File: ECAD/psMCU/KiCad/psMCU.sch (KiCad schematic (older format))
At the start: 0 parts

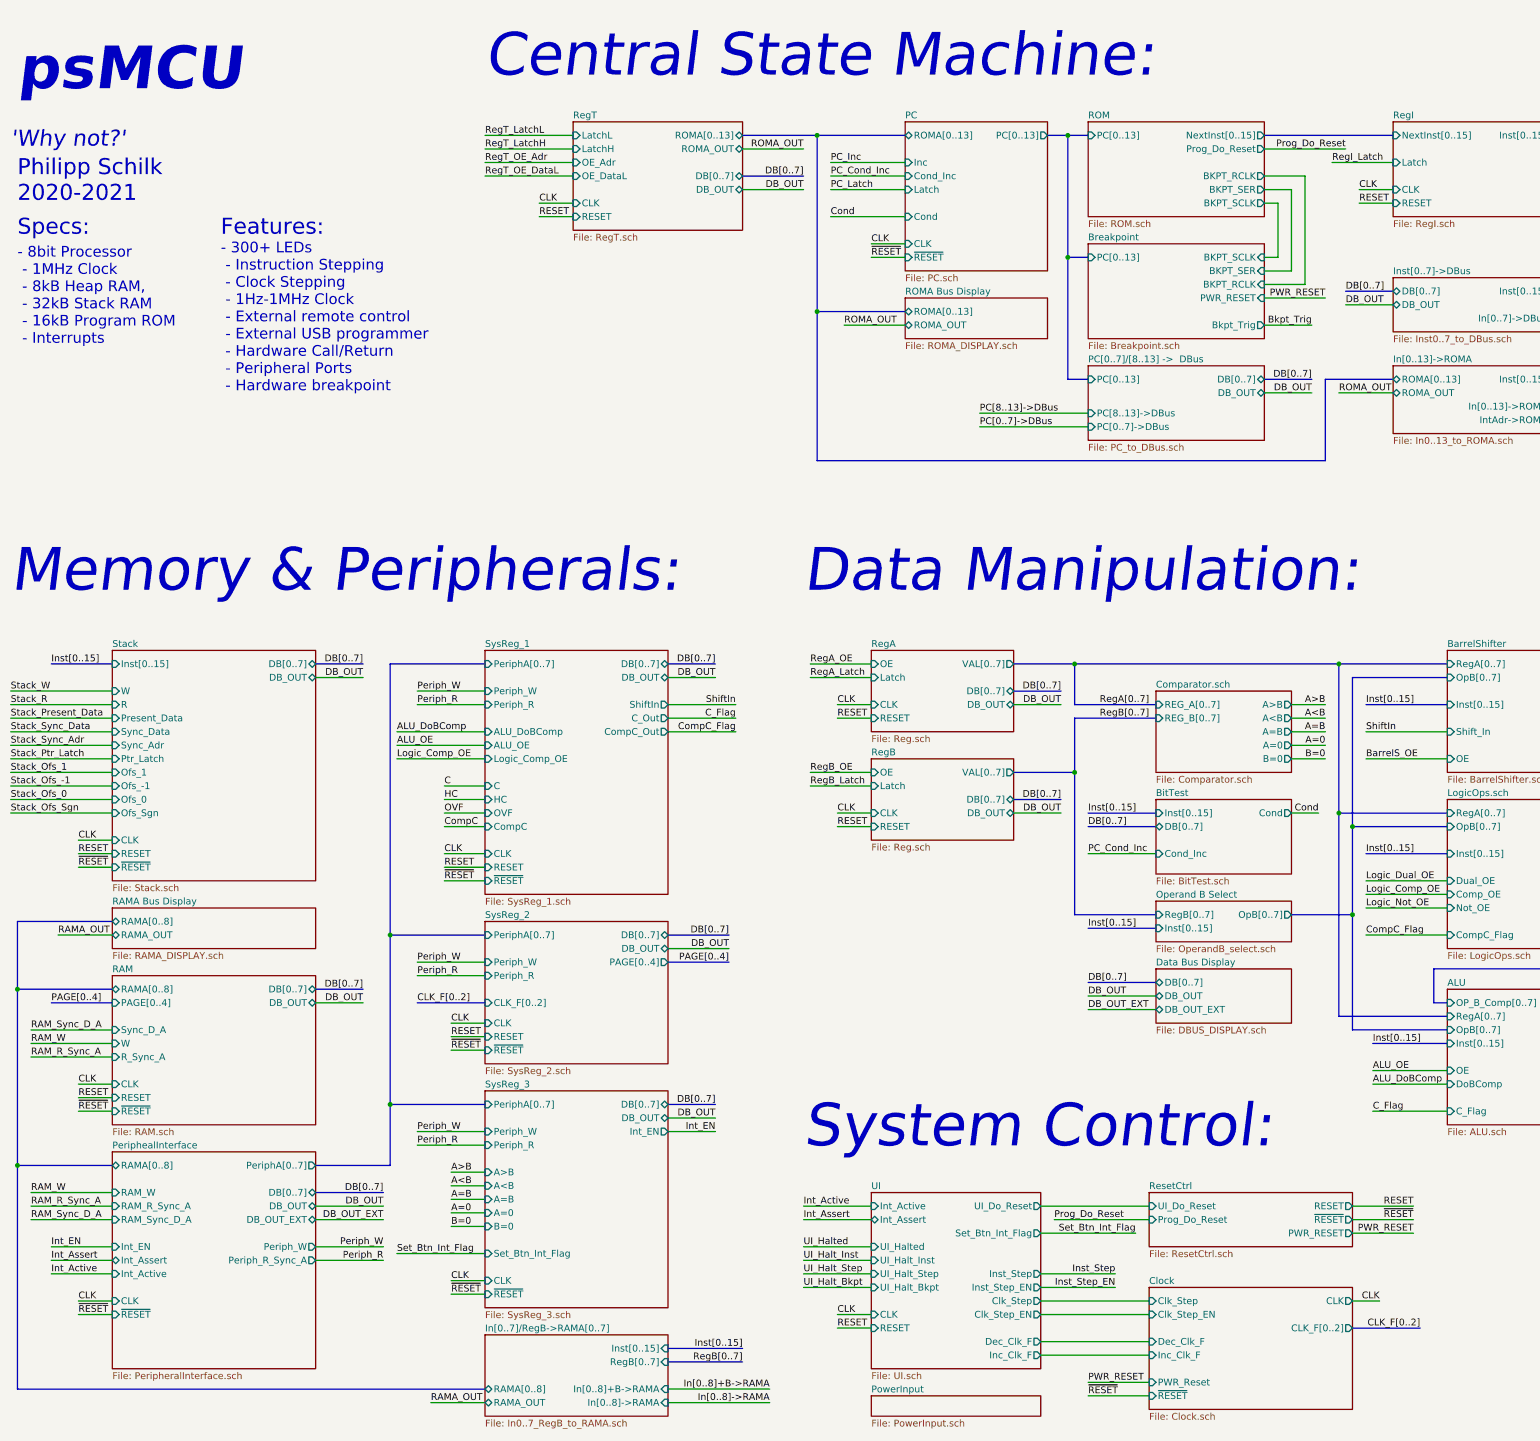
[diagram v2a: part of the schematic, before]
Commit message: Sch: Increased RAM page count, changed SYS registers
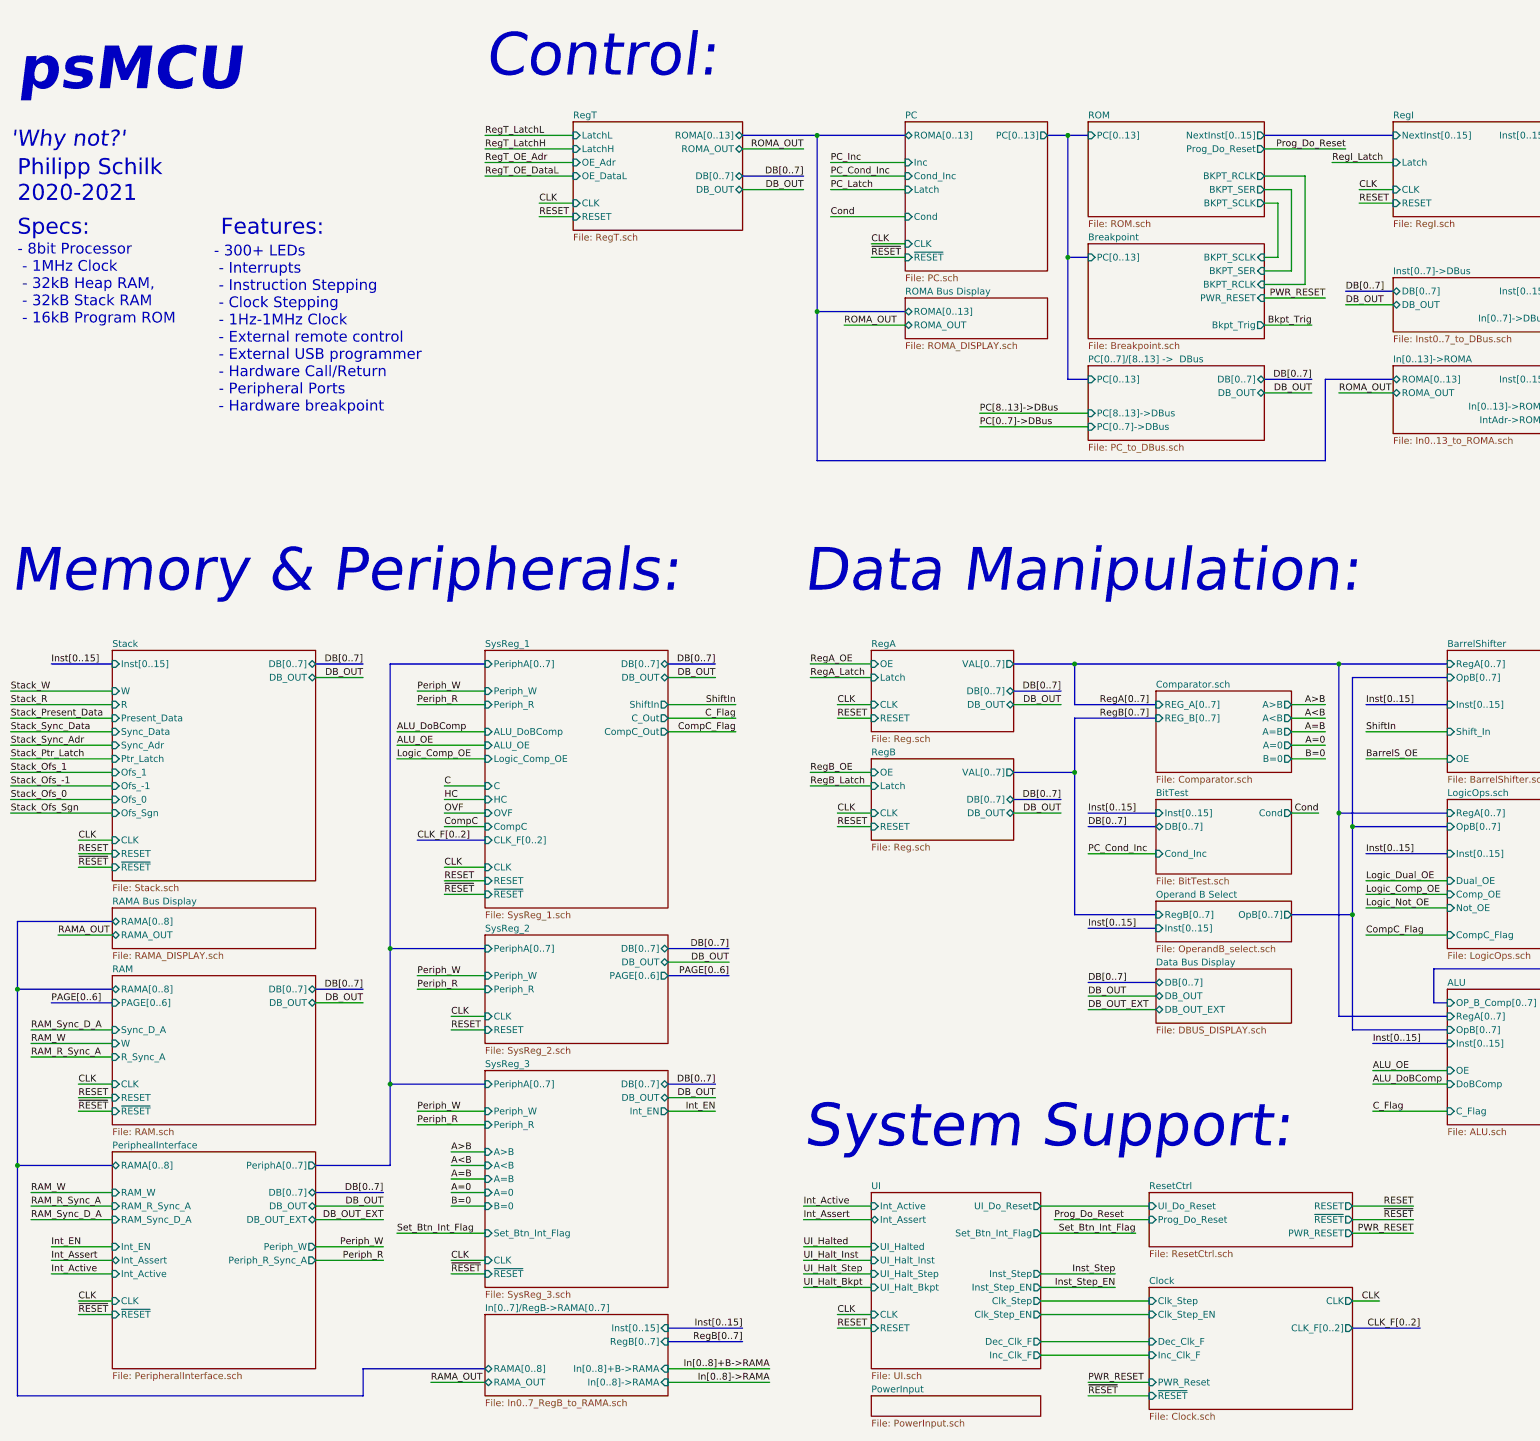
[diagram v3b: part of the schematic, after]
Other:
- note added: "- 300+ LEDs\n - Interrupts\n - Instruction Stepping\n - Clock Stepping\n - 1Hz-1MHz Clock\n - External remote control\n - External USB programmer\n - Hardware Call/Return\n - Peripheral Ports\n - Hardware breakpoint"
- note added: "- 8bit Processor\n - 1MHz Clock\n - 32kB Heap RAM, \n - 32kB Stack RAM\n - 16kB Program ROM\n"
- note added: "Control:"
- note added: "System Support:"
- note removed: "- 300+ LEDs\n - Instruction Stepping\n - Clock Stepping\n - 1Hz-1MHz Clock\n - External remote control\n - External USB programmer\n - Hardware Call/Return\n - Peripheral Ports\n - Hardware breakpoint"
- note removed: "- 8bit Processor\n - 1MHz Clock\n - 8kB Heap RAM, \n - 32kB Stack RAM\n - 16kB Program ROM\n - Interrupts"
- note removed: "Central State Machine:"
- note removed: "System Control:"

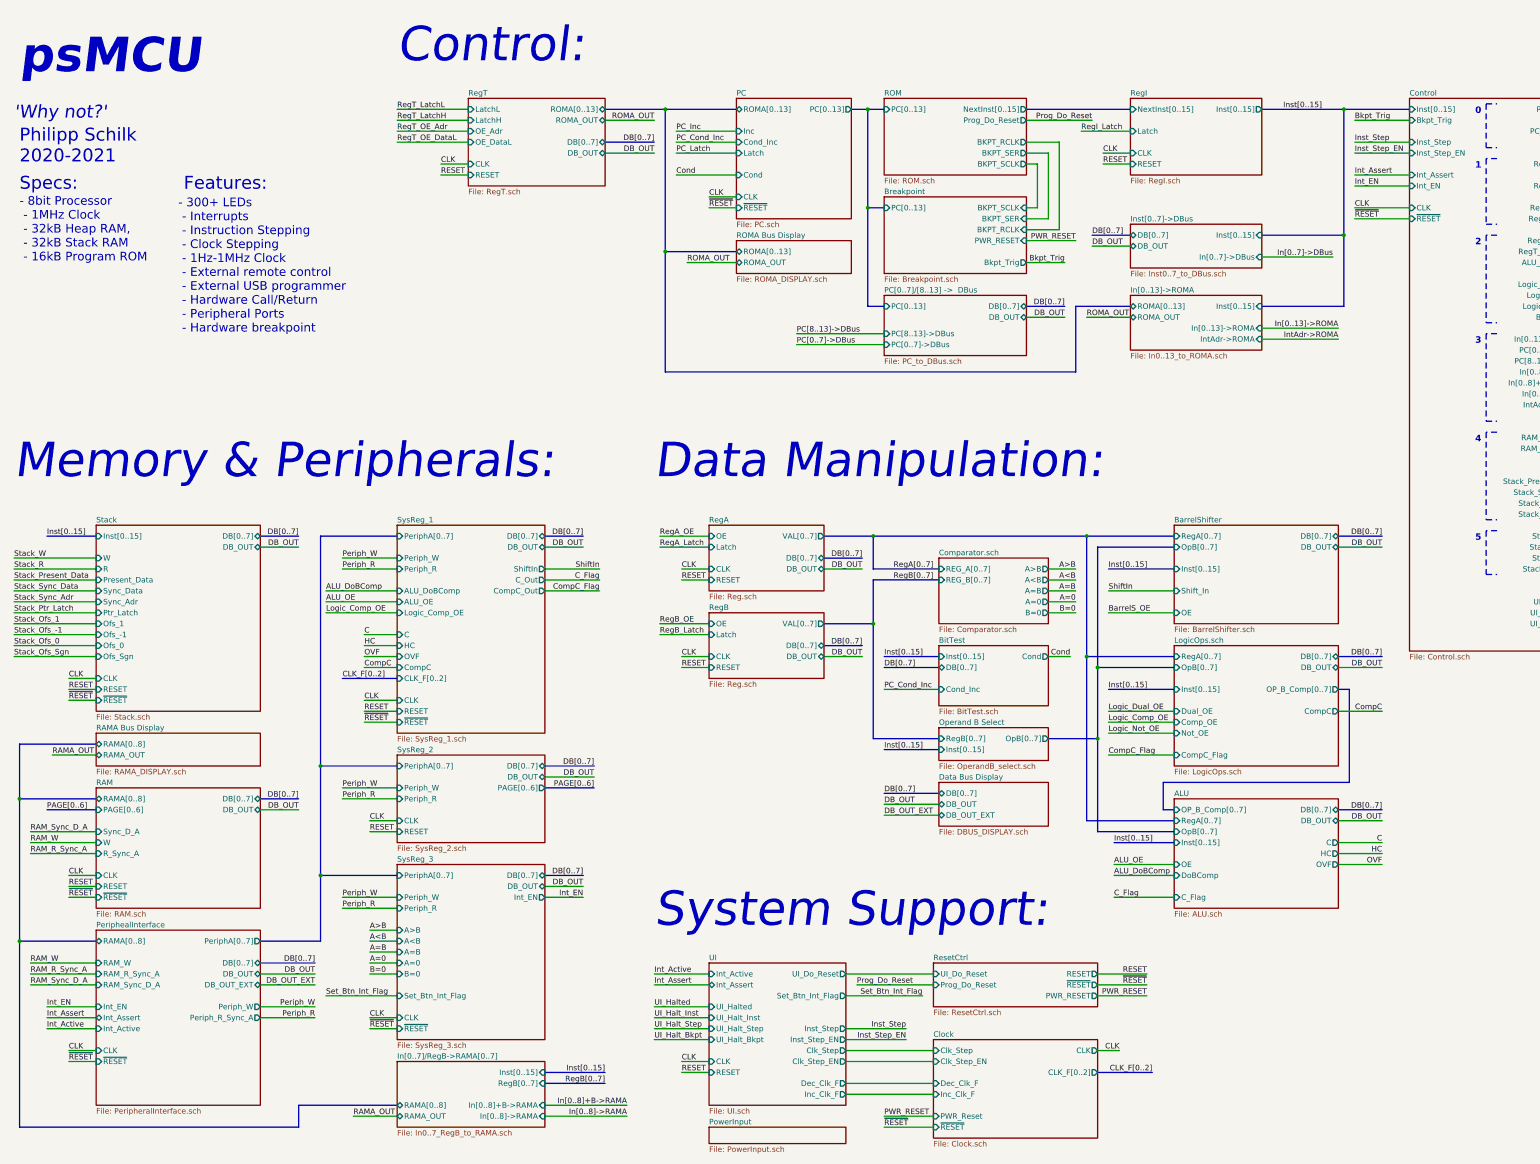
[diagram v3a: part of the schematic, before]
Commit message: Sch: Improved Clk/Reset distribution, moved to global labels
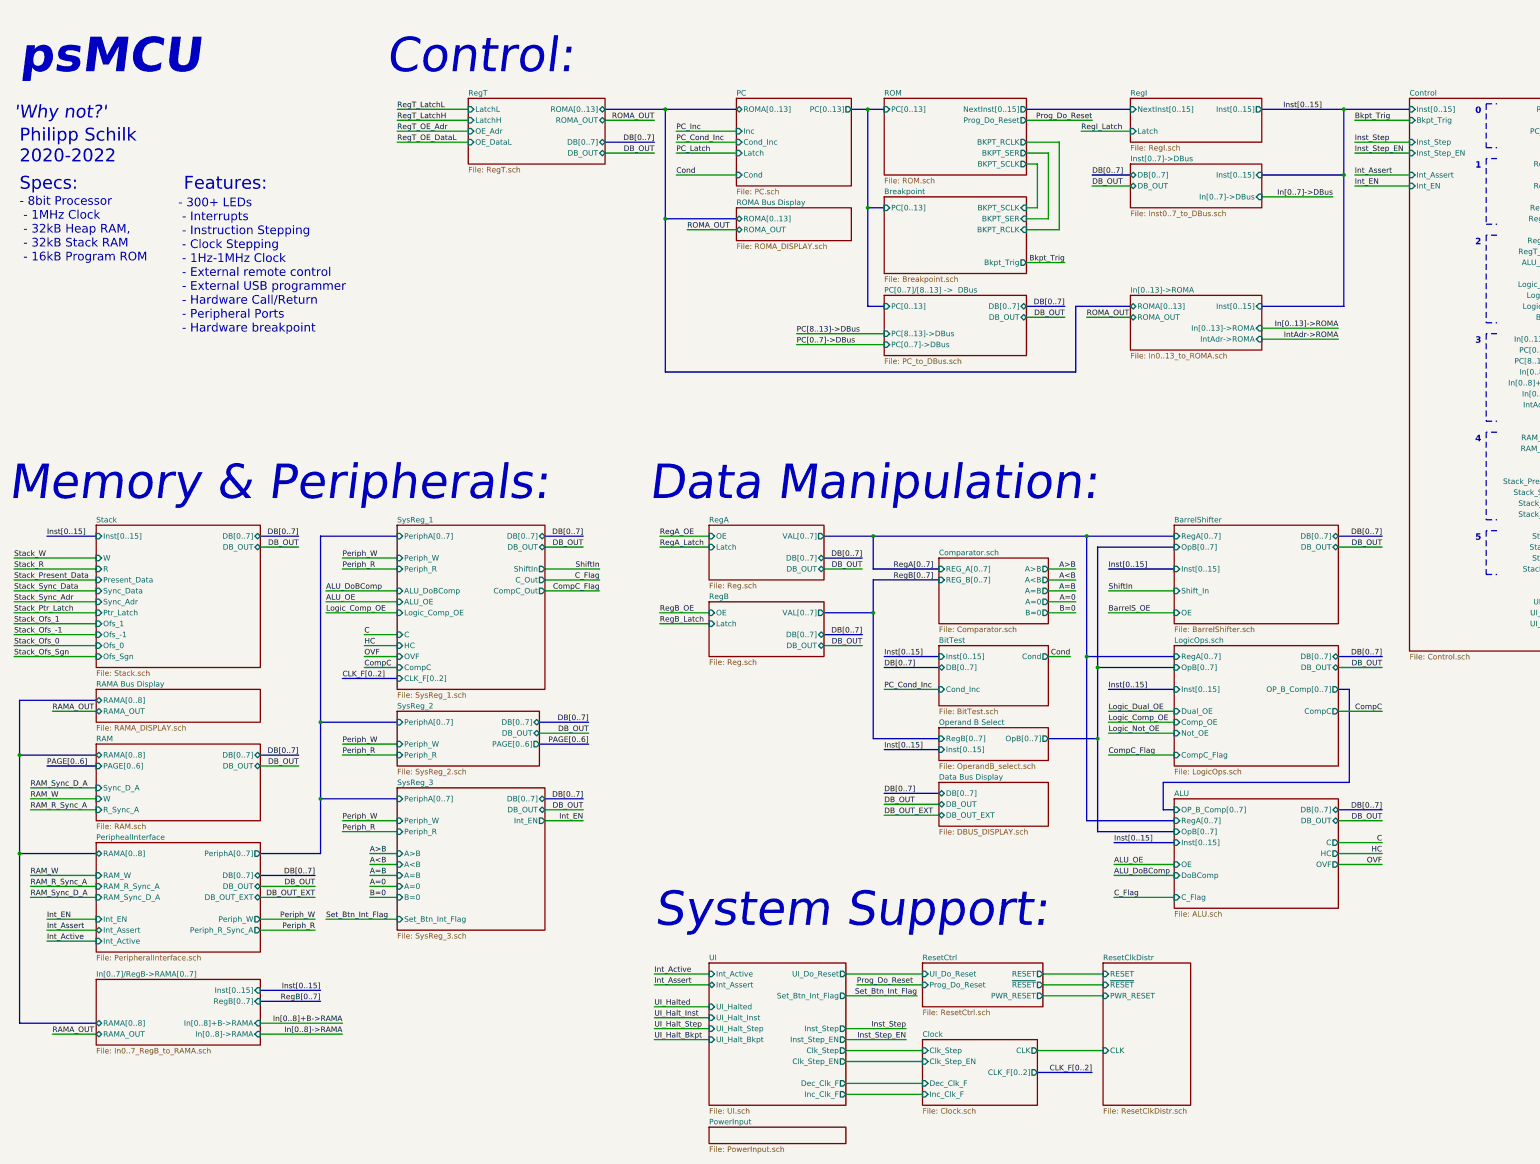
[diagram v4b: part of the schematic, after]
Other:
- note added: "Philipp Schilk\n2020-2022"
- note removed: "Philipp Schilk\n2020-2021"
